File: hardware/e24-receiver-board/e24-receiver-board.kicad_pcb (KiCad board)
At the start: 2 copper layers, 24 x 8.6 mm, 21 parts, among them J1 505070-2422, J10 SPEAKER-, J11 GND1, J12 TRACK_RIGHT, J13 MOTOR+, J14 LAMP_REAR, J15 CAP+, J16 U+, J17 AUX3, J18 AUX10, J19 AUX12, J2 TRACK_LEFT, J20 SPEAKER+, J21 GND2, J3 MOTOR-, J4 LAMP_FRONT, J5 VCC, J6 AUX1, J7 AUX2, J8 AUX4, J9 AUX11

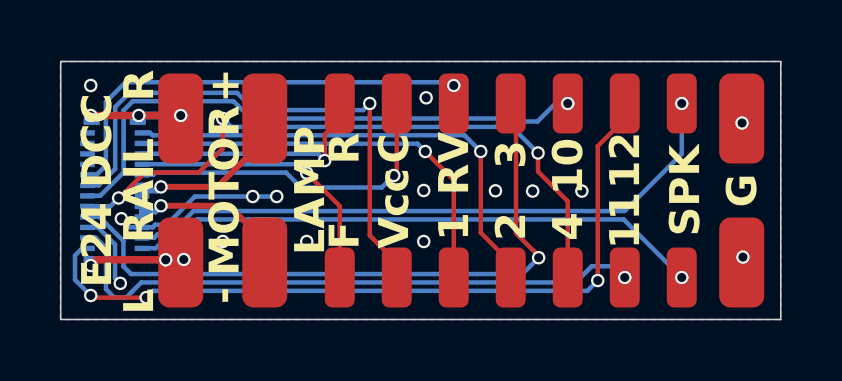
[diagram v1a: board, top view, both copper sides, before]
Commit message: fix: un-swap aux11/aux12 pins
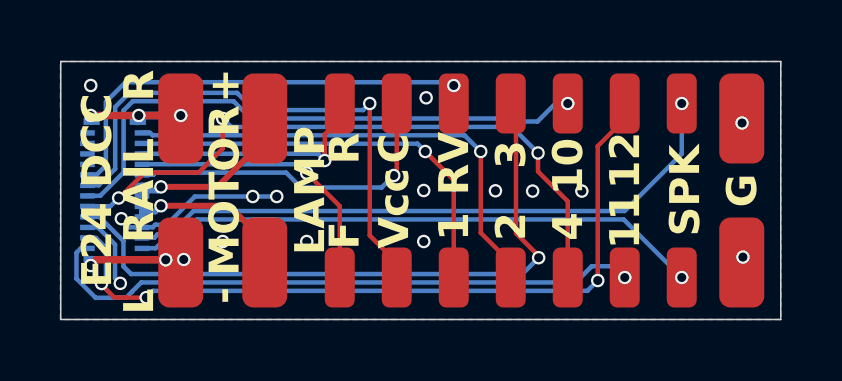
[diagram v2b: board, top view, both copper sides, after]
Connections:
- J1 pad 23: /AUX11 -> /AUX12
- J1 pad 24: /AUX12 -> /AUX11
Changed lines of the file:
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@@
 			(size 0.18 0.49)
 			(layers "B.Cu" "B.Mask" "B.Paste")
-			(net 8 "/AUX11")
+			(net 16 "/AUX12")
 			(pinfunction "23")
 			(pintype "passive")
@@
 			(size 0.18 0.49)
 			(layers "B.Cu" "B.Mask" "B.Paste")
-			(net 16 "/AUX12")
+			(net 8 "/AUX11")
 			(pinfunction "24")
 			(pintype "passive")
@@
 	)
 	(segment
+		(start 130.574 72.587488)
+		(end 130.574 71.726)
+		(width 0.15)
+		(layer "B.Cu")
+		(net 8)
+	)
+	(segment
+		(start 132.231752 73.22)
+		(end 131.838248 73.22)
+		(width 0.15)
+		(layer "B.Cu")
+		(net 8)
+	)
+	(segment
+		(start 132.733248 72.715)
+		(end 132.425 73.023248)
+		(width 0.15)
+		(layer "B.Cu")
+		(net 8)
+	)
+	(segment
+		(start 148.85 72.55)
+		(end 148.475 72.175)
+		(width 0.15)
+		(layer "B.Cu")
+		(net 8)
+	)
+	(segment
+		(start 147.753248 72.175)
+		(end 147.213248 72.715)
+		(width 0.15)
+		(layer "B.Cu")
+		(net 8)
+	)
+	(segment
+		(start 130.72 71.58)
+		(end 130.94 71.58)
+		(width 0.15)
+		(layer "B.Cu")
+		(net 8)
+	)
+	(segment
+		(start 131.838248 73.22)
+		(end 131.831906 73.226342)
+		(width 0.15)
+		(layer "B.Cu")
+		(net 8)
+	)
+	(segment
+		(start 147.213248 72.715)
+		(end 132.733248 72.715)
+		(width 0.15)
+		(layer "B.Cu")
+		(net 8)
+	)
+	(segment
+		(start 131.212854 73.226342)
+		(end 130.574 72.587488)
+		(width 0.15)
+		(layer "B.Cu")
+		(net 8)
+	)
+	(segment
+		(start 132.425 73.023248)
+		(end 132.425 73.026752)
+		(width 0.15)
+		(layer "B.Cu")
+		(net 8)
+	)
+	(segment
+		(start 130.574 71.726)
+		(end 130.72 71.58)
+		(width 0.15)
+		(layer "B.Cu")
+		(net 8)
+	)
+	(segment
+		(start 131.831906 73.226342)
+		(end 131.212854 73.226342)
+		(width 0.15)
+		(layer "B.Cu")
+		(net 8)
+	)
+	(segment
 		(start 132.425 73.026752)
 		(end 132.231752 73.22)
@@
 	)
 	(segment
-		(start 147.213248 72.715)
-		(end 132.733248 72.715)
-		(width 0.15)
-		(layer "B.Cu")
-		(net 8)
-	)
-	(segment
-		(start 147.753248 72.175)
-		(end 147.213248 72.715)
-		(width 0.15)
-		(layer "B.Cu")
-		(net 8)
-	)
-	(segment
-		(start 131.215 71.225)
-		(end 130.942 71.225)
-		(width 0.15)
-		(layer "B.Cu")
-		(net 8)
-	)
-	(segment
-		(start 132.733248 72.715)
-		(end 132.425 73.023248)
-		(width 0.15)
-		(layer "B.Cu")
-		(net 8)
-	)
-	(segment
-		(start 132.231752 73.22)
-		(end 131.838248 73.22)
-		(width 0.15)
-		(layer "B.Cu")
-		(net 8)
-	)
-	(segment
-		(start 131.56 71.57)
-		(end 131.215 71.225)
-		(width 0.15)
-		(layer "B.Cu")
-		(net 8)
-	)
-	(segment
 		(start 148.475 72.175)
 		(end 147.753248 72.175)
-		(width 0.15)
-		(layer "B.Cu")
-		(net 8)
-	)
-	(segment
-		(start 148.85 72.55)
-		(end 148.475 72.175)
-		(width 0.15)
-		(layer "B.Cu")
-		(net 8)
-	)
-	(segment
-		(start 131.838248 73.22)
-		(end 131.56 72.941752)
-		(width 0.15)
-		(layer "B.Cu")
-		(net 8)
-	)
-	(segment
-		(start 132.425 73.023248)
-		(end 132.425 73.026752)
-		(width 0.15)
-		(layer "B.Cu")
-		(net 8)
-	)
-	(segment
-		(start 131.56 72.941752)
-		(end 131.56 71.57)
 		(width 0.15)
 		(layer "B.Cu")
@@
 	)
 	(segment
-		(start 131.05 73.15)
-		(end 131.12 73.22)
+		(start 132.232166 73.221)
+		(end 132.233166 73.22)
 		(width 0.15)
 		(layer "F.Cu")
@@
 	)
 	(segment
-		(start 131.12 73.22)
+		(start 132.233166 73.22)
 		(end 132.9 73.22)
 		(width 0.15)
@@
 	)
 	(segment
+		(start 131.41002 72.750342)
+		(end 131.41002 72.793186)
+		(width 0.15)
+		(layer "F.Cu")
+		(net 16)
+	)
+	(segment
+		(start 131.837834 73.221)
+		(end 132.232166 73.221)
+		(width 0.15)
+		(layer "F.Cu")
+		(net 16)
+	)
+	(segment
 		(start 148.85 67.27)
 		(end 148.85 66.75)
@@
 		(net 16)
 	)
-	(via
-		(at 131.05 73.15)
-		(size 0.45)
-		(drill 0.3)
-		(layers "F.Cu" "B.Cu")
+	(segment
+		(start 131.41002 72.793186)
+		(end 131.837834 73.221)
+		(width 0.15)
+		(layer "F.Cu")
 		(net 16)
 	)
 	(via
+		(at 131.41002 72.750342)
+		(size 0.45)
+		(drill 0.3)
+		(layers "F.Cu" "B.Cu")
+		(net 16)
+	)
+	(via
 		(at 147.95 72.65)
 		(size 0.45)
@@
 		(drill 0.3)
 		(layers "F.Cu" "B.Cu")
+		(net 16)
+	)
+	(segment
+		(start 131.556 72.604362)
+		(end 131.556 71.566)
+		(width 0.15)
+		(layer "B.Cu")
 		(net 16)
 	)
@@
 	)
 	(segment
-		(start 130.525 72.625)
-		(end 130.525 71.815)
+		(start 131.41002 72.750342)
+		(end 131.556 72.604362)
 		(width 0.15)
 		(layer "B.Cu")
@@
 	)
 	(segment
-		(start 130.765 71.575)
-		(end 130.942 71.575)
-		(width 0.15)
-		(layer "B.Cu")
-		(net 16)
-	)
-	(segment
-		(start 130.525 71.815)
-		(end 130.765 71.575)
+		(start 131.556 71.566)
+		(end 131.22 71.23)
 		(width 0.15)
 		(layer "B.Cu")
@@
 	)
 	(segment
-		(start 131.05 73.15)
-		(end 130.525 72.625)
-		(width 0.15)
-		(layer "B.Cu")
+		(start 131.22 71.23)
+		(end 130.94 71.23)
+		(width 0.15)
+		(layer "B.Cu")
